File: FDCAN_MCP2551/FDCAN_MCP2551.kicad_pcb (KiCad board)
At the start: 2 copper layers, 4 parts, among them J1 Conn_01x06_Male, U1 MCP2551-I-SN

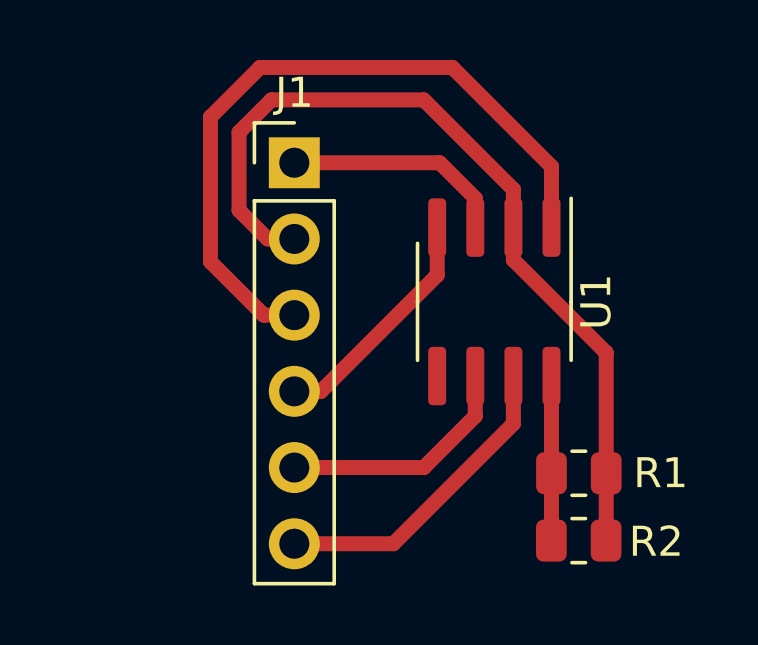
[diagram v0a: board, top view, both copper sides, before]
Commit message: esqueatico circuito BMS para monitoramento de temperatura
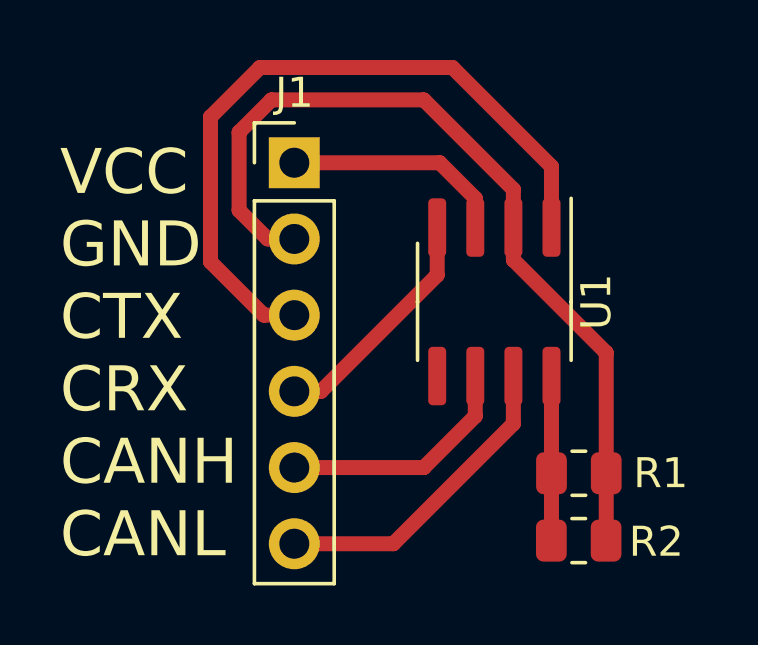
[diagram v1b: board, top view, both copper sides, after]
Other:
- board text added: "VCC GND CTX CRX CANH CANL"
